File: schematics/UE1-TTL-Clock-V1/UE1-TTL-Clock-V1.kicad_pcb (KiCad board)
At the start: 2 copper layers, 76.8 x 99.1 mm, 82 parts, among them J1 Edge 1, J2 Edge 2, SW1 RUN, SW2 HALT, SW3 RESET, U1 74LS74, U2 74HC4017, U3 NE555, U4 NE555, U5 74LS132, U6 74LS02

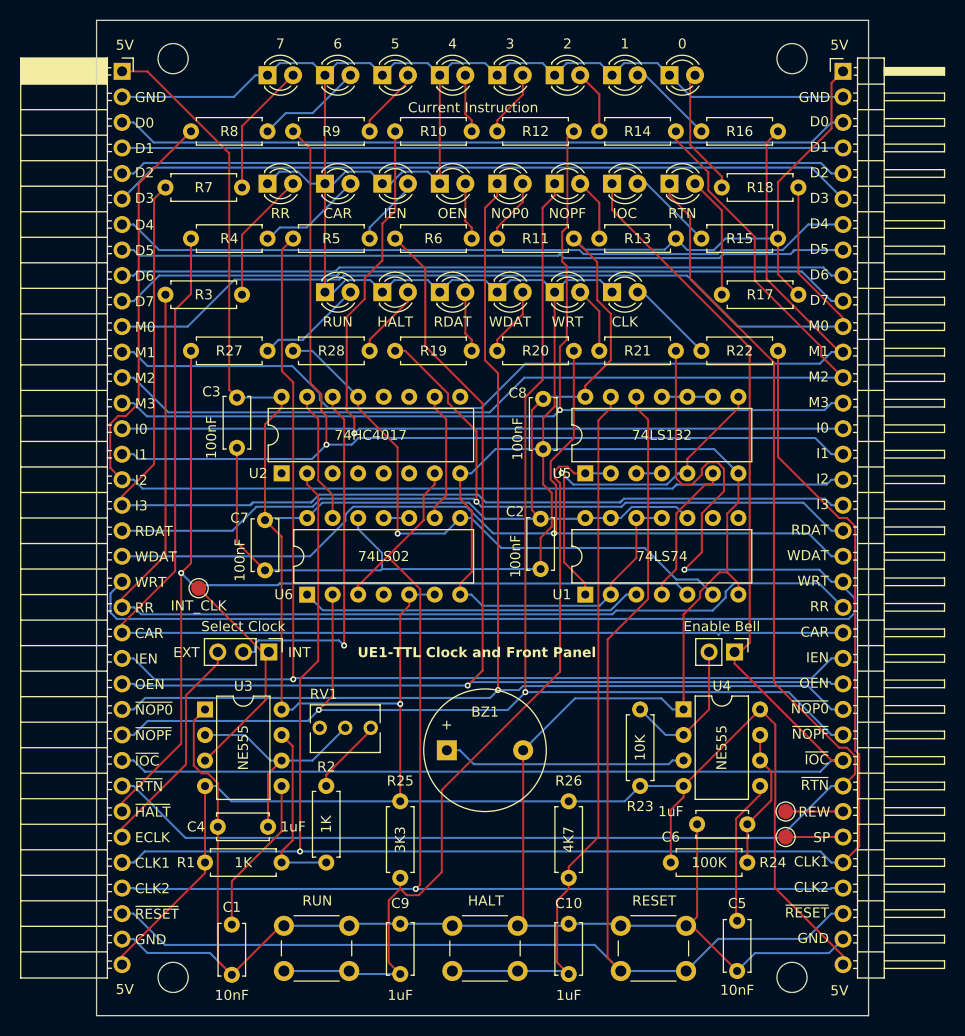
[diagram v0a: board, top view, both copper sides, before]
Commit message: Update the clock schematic with V2 modifications
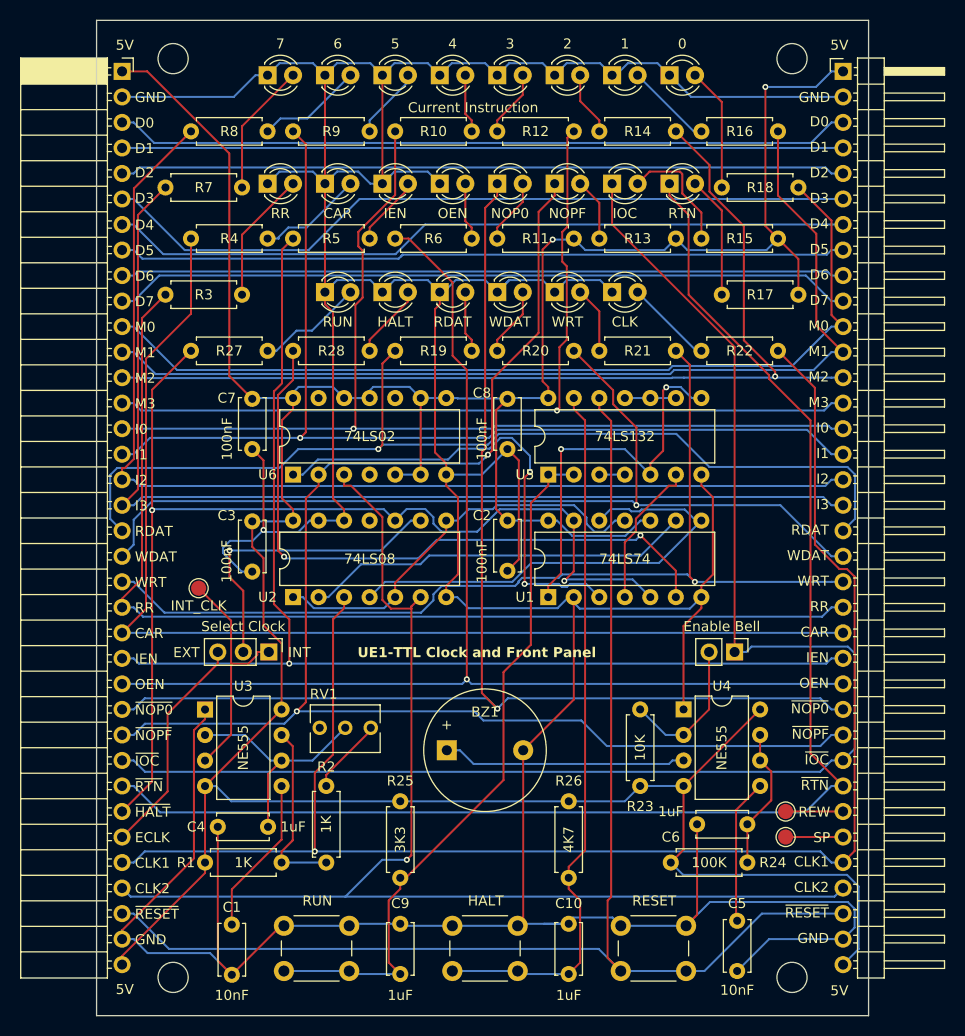
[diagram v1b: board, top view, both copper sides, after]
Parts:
- U2: value 74HC4017 -> 74LS08; footprint Package_DIP:DIP-16_W7.62mm -> Package_DIP:DIP-14_W7.62mm
- moved C3 12.4 mm to (103.1, 98.1)
- moved U2 12.4 mm to (107.2, 105.7)
- moved C7 12.1 mm to (103.1, 85.9)
- moved U6 12.0 mm to (107.2, 93.5)
- moved U1 3.70 mm to (132.6, 105.7)
- moved U5 3.69 mm to (132.6, 93.5)
- moved C8 3.56 mm to (128.5, 85.9)
- moved C2 3.31 mm to (128.5, 98.0)
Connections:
- U1 pad 11: GND -> Net-(U1B-C)
- U1 pad 12: GND -> Net-(U1B-D)
- U1 pad 13: +5V -> ~{HALTED}
- U1 pad 8: unconnected-(U1B-~{Q}-Pad8) -> Net-(U1B-D)
- U1 pad 9: unconnected-(U1B-Q-Pad9) -> Net-(U1B-Q)
- U2 pad 1: unconnected-(U2-Q5-Pad1) -> Net-(U1B-C)
- U2 pad 10: Net-(U2-Q4) -> ~{HALTED}
- U2 pad 12: unconnected-(U2-Cout-Pad12) -> GND
- U2 pad 13: ~{RUNNING} -> GND
- U2 pad 14: MAIN_CLK -> +5V
- U2 pad 2: CLK1 -> Net-(U1B-Q)
- U2 pad 3: unconnected-(U2-Q0-Pad3) -> CLK1
- U2 pad 4: unconnected-(U2-Q2-Pad4) -> Net-(U1B-D)
- U2 pad 5: unconnected-(U2-Q6-Pad5) -> Net-(U1B-C)
- U2 pad 6: unconnected-(U2-Q7-Pad6) -> CLK2
- U2 pad 7: CLK2 -> GND
- U2 pad 8: GND -> Net-(U1B-C)
- U2 pad 9: unconnected-(U2-Q8-Pad9) -> MAIN_CLK
- U6 pad 10: Net-(U6-Pad10) -> unconnected-(U6-Pad10)
- U6 pad 11: Net-(U6-Pad10) -> +5V
- U6 pad 12: GND -> +5V
- U6 pad 13: Net-(U2-Reset) -> unconnected-(U6-Pad13)
- U6 pad 8: ~{RUNNING} -> +5V
- U6 pad 9: Net-(U2-Q4) -> +5V
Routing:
- net Net-(U1B-D): track 0.00 -> 47.4 mm
- net Net-(U1B-C): track 0.00 -> 41.1 mm
- net Net-(U1B-Q): track 0.00 -> 38.7 mm
- net WRITE: track 129.1 -> 99.7 mm
- net Net-(U2-Reset): track 13.1 -> 0.00 mm
- net Net-(U2-Q4): track 13.0 -> 0.00 mm
- net Net-(U1A-C): track 34.1 -> 47.0 mm, vias 0 -> 2
- net CLK1: track 166.9 -> 154.2 mm
- net GND: track 495.2 -> 506.9 mm, vias 0 -> 1
- net ~{HALTED}: track 100.3 -> 110.3 mm, vias 1 -> 2
- net +5V: track 357.3 -> 348.1 mm, vias 1 -> 2
- net ~{OP_NOPF}: track 139.2 -> 146.5 mm
- net ~{RUNNING}: track 58.8 -> 66.0 mm, vias 1 -> 2
- net Net-(C9-Pad1): track 78.7 -> 71.6 mm
- net RD_DATA: track 93.7 -> 100.1 mm
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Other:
- board text added: "Design by Rhys Weatherley, Version 1, July 2025"
- board text removed: "Design by Rhys Weatherley, Version 2, July 2025"
